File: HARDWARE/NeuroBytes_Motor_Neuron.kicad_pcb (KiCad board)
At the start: 2 copper layers, 51.2 x 28.4 mm, 28 parts, among them P1 JST_GH_4POS, P2 JST_GH_4POS, P3 JST_GH_4POS, P4 SERVO_CONN, P5 SERVO_CONN, P6 JST_GH_5-pos, Q1 MMBT3904, Q2 MMBT3904, Q3 MMBT3904, SW1 SW_PUSH, U1 STM32L011Gx, U2 LD3985G33R

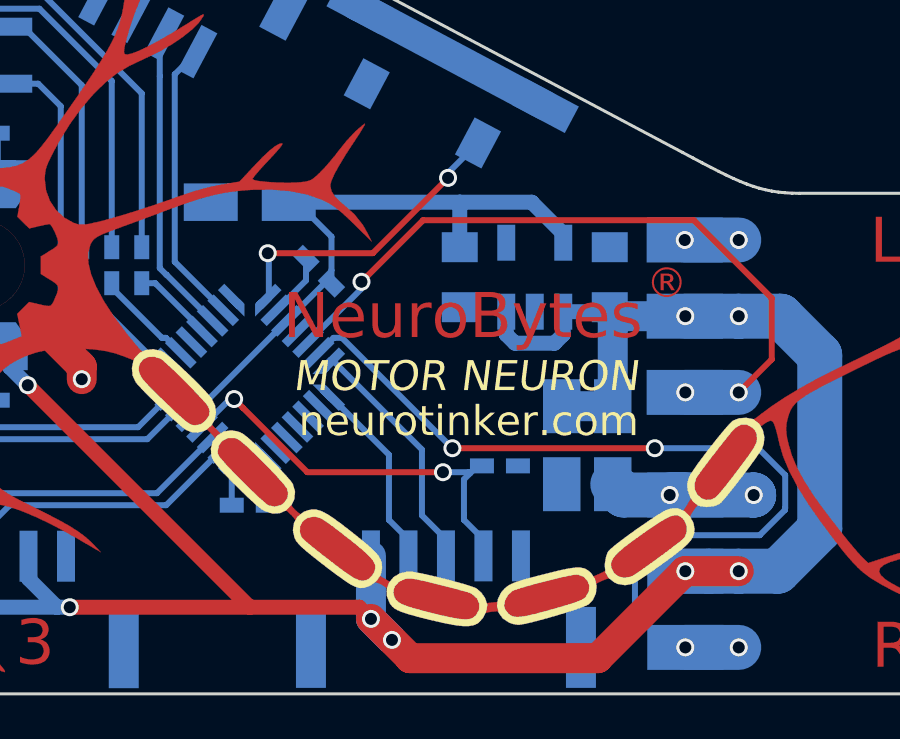
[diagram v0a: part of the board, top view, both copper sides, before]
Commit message: added ESD protection. minor routing changes. updated title block.
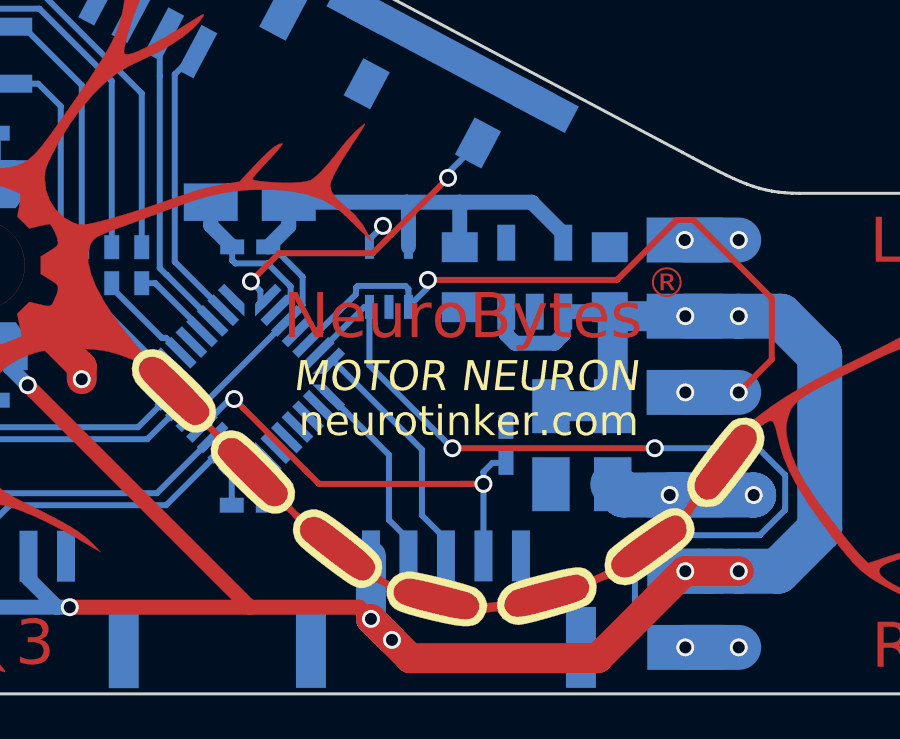
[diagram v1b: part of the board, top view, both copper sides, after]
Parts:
- added U3: RClamp0503F, KiCad_Footprints:ZF_SMD_SOT-353, B.Cu at (190.6, 58.4)
- moved C3 2.42 mm to (186.0, 57.4), turned to 180 degrees
- moved C5 0.73 mm to (194.5, 64.0), turned to 90 degrees
- moved C6 0.36 mm to (196.0, 64.0)
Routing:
- net GND: track 30.0 -> 33.4 mm
- net SERVO_2: track 30.5 -> 32.8 mm
- net RESET: track 14.6 -> 16.5 mm
- net IDENTIFY: track 10.7 -> 12.5 mm, vias 2 -> 3
- net +3V3: track 21.7 -> 23.0 mm
- net SERVO_1: track 23.7 -> 24.8 mm
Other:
- board text removed: "POWER"

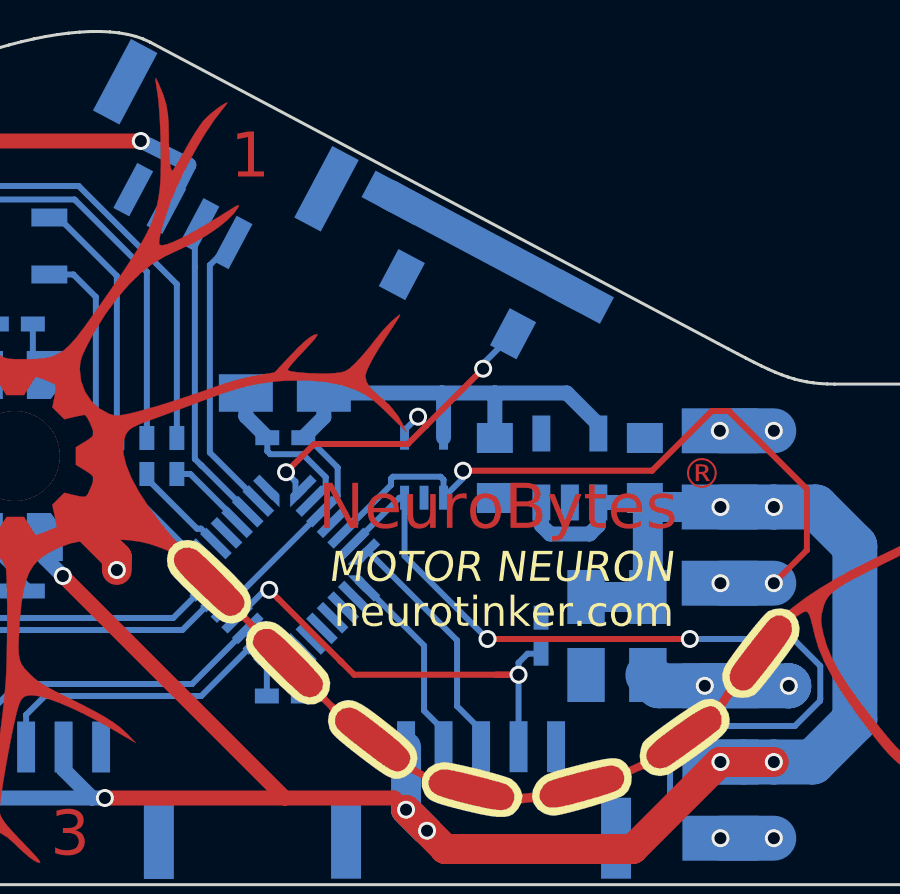
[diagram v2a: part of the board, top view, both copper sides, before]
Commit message: updated footprints to include B.Fab outlines. minor routing changes. re-generated Gerbers. added placement pdf.
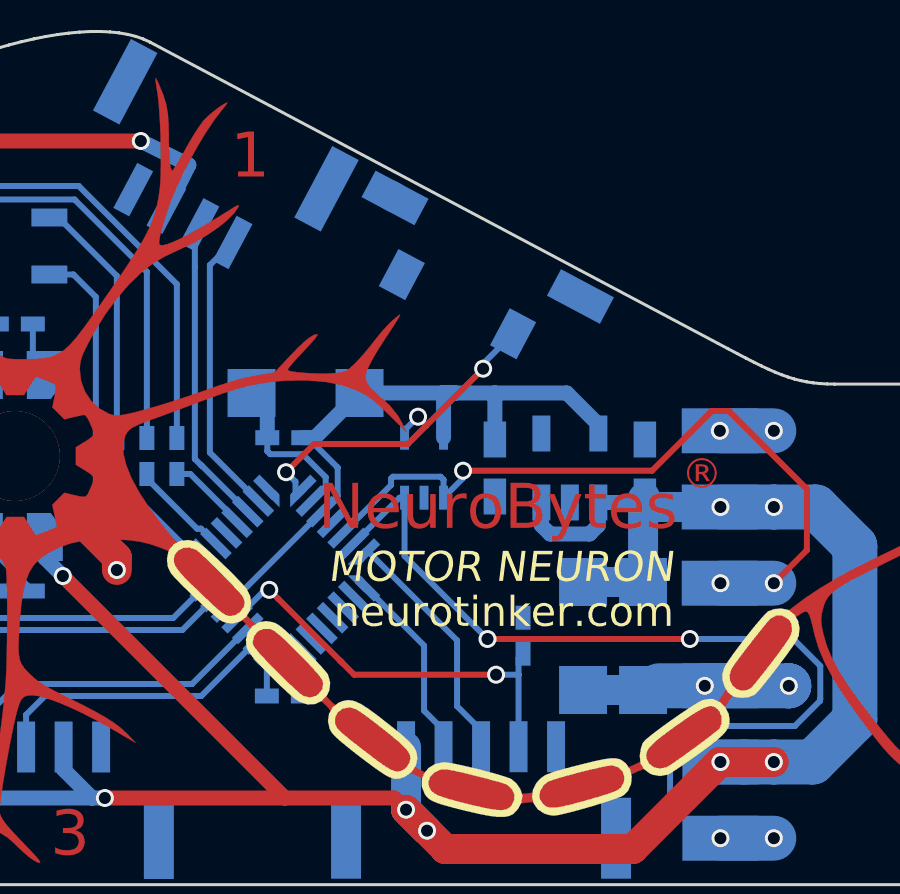
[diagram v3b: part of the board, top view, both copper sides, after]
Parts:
- C1, C4: footprint KiCad_Footprints:ZF_SMD_NonPol_0603 -> Capacitors_SMD:C_0603_HandSoldering
- C6, C7: value 10u -> 22u
- moved C2 0.69 mm to (186.7, 55.9)
- moved C5 0.60 mm to (193.9, 64.0)
- moved C7 0.16 mm to (197.9, 64.0)
- moved C6 0.10 mm to (195.9, 64.0)
- turned U1 to 135 degrees
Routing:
- net GND: track 33.4 -> 27.7 mm
- net RESET: track 16.5 -> 15.3 mm
